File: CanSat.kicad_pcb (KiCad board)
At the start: 2 copper layers, 55.6 x 55.5 mm, 83 parts, among them IC1 W25Q128JVPIQ, J1 USB_C_Receptacle, J10 Conn_01x04_Pin, J11 Conn_01x03_Socket, J2 Conn_Coaxial, J3 Conn_01x06_Socket, J4 Conn_01x02_Pin, J5 Screw_Terminal_01x02, J6 Conn_01x06_Pin, J7 Conn_01x03_Pin, J8 Conn_01x02_Pin, J9 Conn_01x02_Pin, M2 MountingHole_2.2mm_M2, SW1 SW_Push, SW2 SW_Push, SW3 SW_Push, U1 MPU-6050, U3 Waveshare23721, U4 RFM98W-433S2, U5 RP2350_60QFN, U8 BMP280, U9 APS6404L-3SQR-ZR, Y1 Crystal_GND24

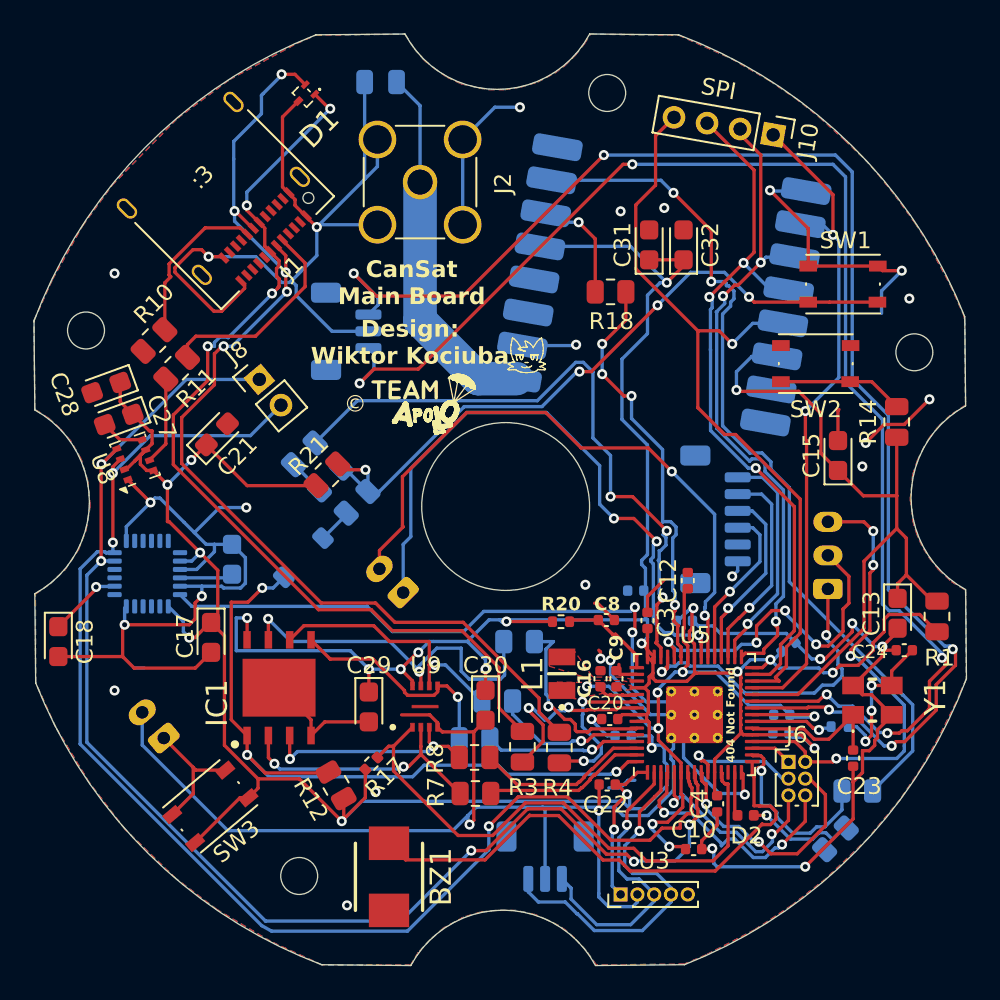
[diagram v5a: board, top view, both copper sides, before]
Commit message: changed buzzer circuit and capacitor footprints
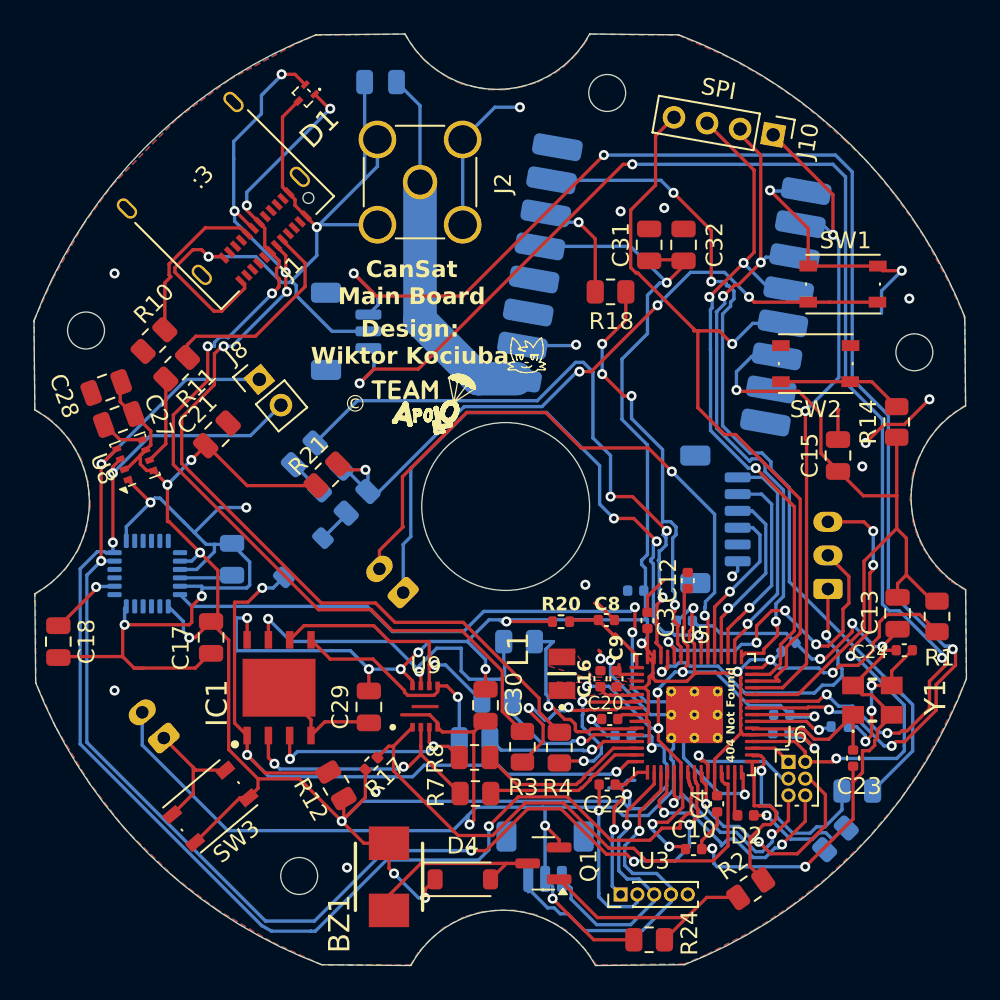
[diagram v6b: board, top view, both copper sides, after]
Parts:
- added D4: MBR0530T1G, Diode_SMD:D_SOD-123, F.Cu at (102.0, 88.2)
- added Q1: Q_NMOS_GSD, Package_TO_SOT_SMD:SOT-23, F.Cu at (106.8, 87.2)
- added R2: 1K, Resistor_SMD:R_0805_2012Metric, F.Cu at (119.2, 88.8)
- added R24: 10K, Resistor_SMD:R_0805_2012Metric, F.Cu at (113.1, 91.8)
- C13, C15, C17, C18, C19, C21, C27, C28, C29, C30, C31, C32: footprint Capacitor_Tantalum_SMD:CP_EIA-2012-15_AVX-P -> Capacitor_SMD:C_0805_2012Metric
- D3: value MBR0530 -> MBR0530T1G
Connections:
- BZ1 pad 1: /BUZZER -> +3V3
- BZ1 pad 2: GND -> Net-(BZ1--)
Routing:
- net /BUZZER: track 31.8 -> 9.39 mm
- net Net-(Q1-G): track 0.00 -> 14.0 mm
- net Net-(BZ1--): track 0.00 -> 11.3 mm
- net GND: track 276.4 -> 285.5 mm, vias 32 -> 34
- net +3V3: track 231.7 -> 239.7 mm, vias 21 -> 23
- net /GPS_RX: track 21.9 -> 22.5 mm

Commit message: added Q1 part number
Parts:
- Q1: value Q_NMOS_GSD -> BSS138
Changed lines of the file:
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@@
 			)
 		)
-		(property "Value" "Q_NMOS_GSD"
+		(property "Value" "BSS138"
 			(at 0 2.4 0)
 			(layer "F.Fab")

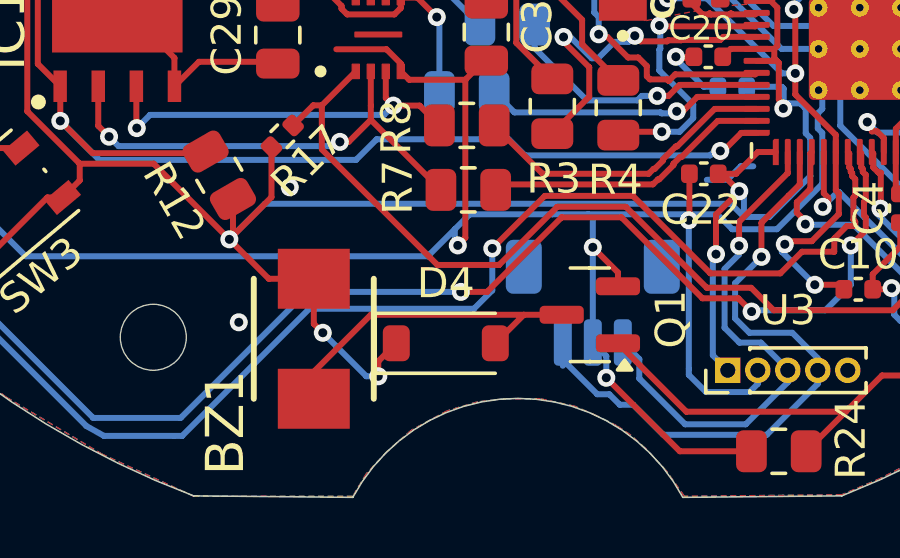
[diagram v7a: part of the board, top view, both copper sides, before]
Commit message: updated spacing
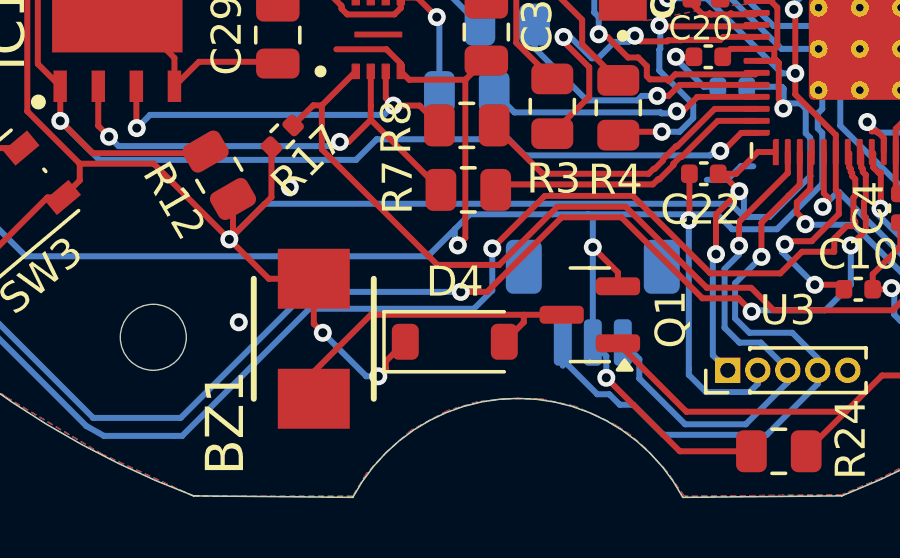
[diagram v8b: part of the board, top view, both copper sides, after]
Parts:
- moved D4 0.30 mm to (102.3, 88.2)
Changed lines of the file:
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@@
 	(footprint "Diode_SMD:D_SOD-123"
 		(layer "F.Cu")
-		(at 102 88.2)
+		(at 102.3 88.15)
 		(descr "SOD-123")
 		(tags "SOD-123")
@@
 	)
 	(segment
+		(start 100 89.05)
+		(end 100 88.8)
+		(width 0.2)
+		(layer "F.Cu")
+		(net 3)
+	)
+	(segment
 		(start 113.325 75.9125)
 		(end 113.1 76.1375)
@@
 	)
 	(segment
-		(start 99.75 88.8)
-		(end 100.35 88.2)
-		(width 0.2)
-		(layer "F.Cu")
-		(net 3)
-	)
-	(segment
 		(start 113.325 75.9125)
 		(end 113.325 76.225)
@@
 	)
 	(segment
+		(start 99.75 89.3)
+		(end 100 89.05)
+		(width 0.2)
+		(layer "F.Cu")
+		(net 3)
+	)
+	(segment
 		(start 118.362644 75.824856)
 		(end 118.450289 75.9125)
@@
 	)
 	(segment
+		(start 100 88.8)
+		(end 100.65 88.15)
+		(width 0.2)
+		(layer "F.Cu")
+		(net 3)
+	)
+	(segment
 		(start 118.549 79.011436)
 		(end 118.549 79.363564)
@@
 	)
 	(segment
-		(start 99.75 89.3)
-		(end 99.75 88.8)
-		(width 0.2)
-		(layer "F.Cu")
-		(net 3)
-	)
-	(segment
 		(start 118.572936 77.3875)
 		(end 118.549 77.411436)
@@
 	)
 	(segment
+		(start 104.6 87.5)
+		(end 103.95 88.15)
+		(width 0.2)
+		(layer "F.Cu")
+		(net 108)
+	)
+	(segment
 		(start 104.6 87.25)
 		(end 99.5 87.25)
@@
 	)
 	(segment
-		(start 103.65 88.2)
-		(end 104.6 87.25)
+		(start 104.6 87.25)
+		(end 104.6 87.5)
 		(width 0.2)
 		(layer "F.Cu")
